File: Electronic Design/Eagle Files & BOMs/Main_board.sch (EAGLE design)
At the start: 49 parts, among them IC2 ATMEGA328-PU, IC3 LM2576S, Q1 BSS192P, Q2 FQD7P20, X1 16MHz

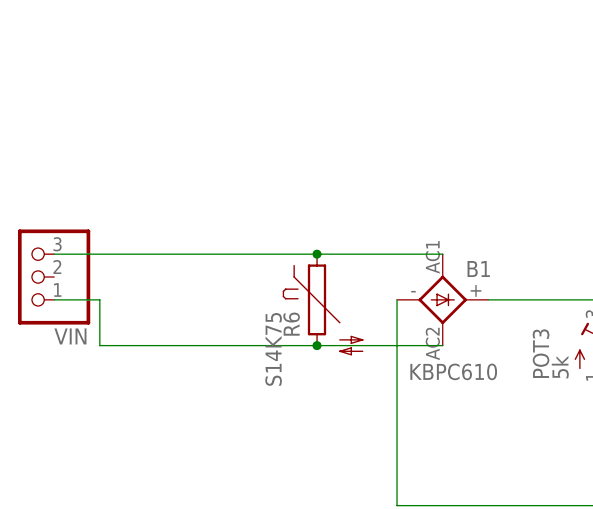
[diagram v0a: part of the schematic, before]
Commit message: Moving everything into postion and adding fuse to start of circuit
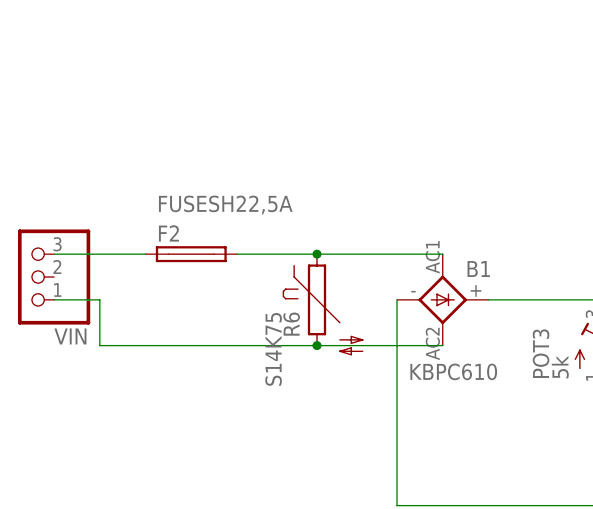
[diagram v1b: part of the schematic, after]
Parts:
- added F2: FUSESH22,5A, fuse:FUSESH22,5A
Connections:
- new net N$1: F2.1, VIN.3
- net VIN_AC1: now also F2.2; no longer VIN.3
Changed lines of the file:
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@@
 <part name="Q1" library="Samson" deviceset="BSS192P" device=""/>
 <part name="Q2" library="Samson" deviceset="FQD7P20" device=""/>
+<part name="F2" library="fuse" deviceset="FUSE" device="SH22,5A" value="FUSESH22,5A"/>
 </parts>
 <sheets>
@@
 <instance part="Q1" gate="G$1" x="-52.07" y="81.28" rot="MR180"/>
 <instance part="Q2" gate="G$1" x="-41.91" y="86.36" rot="R90"/>
+<instance part="F2" gate="G$1" x="-111.76" y="93.98" smashed="yes">
+<attribute name="NAME" x="-115.57" y="95.377" size="1.778" layer="95"/>
+<attribute name="VALUE" x="-115.57" y="98.679" size="1.778" layer="96"/>
+</instance>
 </instances>
 <busses>
@@
 <net name="VIN_AC1" class="0">
 <segment>
-<pinref part="VIN" gate="A" pin="3"/>
-<wire x1="-127" y1="93.98" x2="-97.79" y2="93.98" width="0.1524" layer="91"/>
 <pinref part="R6" gate="G$1" pin="1"/>
 <pinref part="B1" gate="1" pin="AC1"/>
 <wire x1="-83.82" y1="93.98" x2="-97.79" y2="93.98" width="0.1524" layer="91"/>
+<pinref part="F2" gate="G$1" pin="2"/>
+<wire x1="-106.68" y1="93.98" x2="-97.79" y2="93.98" width="0.1524" layer="91"/>
 <junction x="-97.79" y="93.98"/>
 </segment>
@@
 </segment>
 </net>
+<net name="N$1" class="0">
+<segment>
+<pinref part="VIN" gate="A" pin="3"/>
+<pinref part="F2" gate="G$1" pin="1"/>
+<wire x1="-127" y1="93.98" x2="-116.84" y2="93.98" width="0.1524" layer="91"/>
+</segment>
+</net>

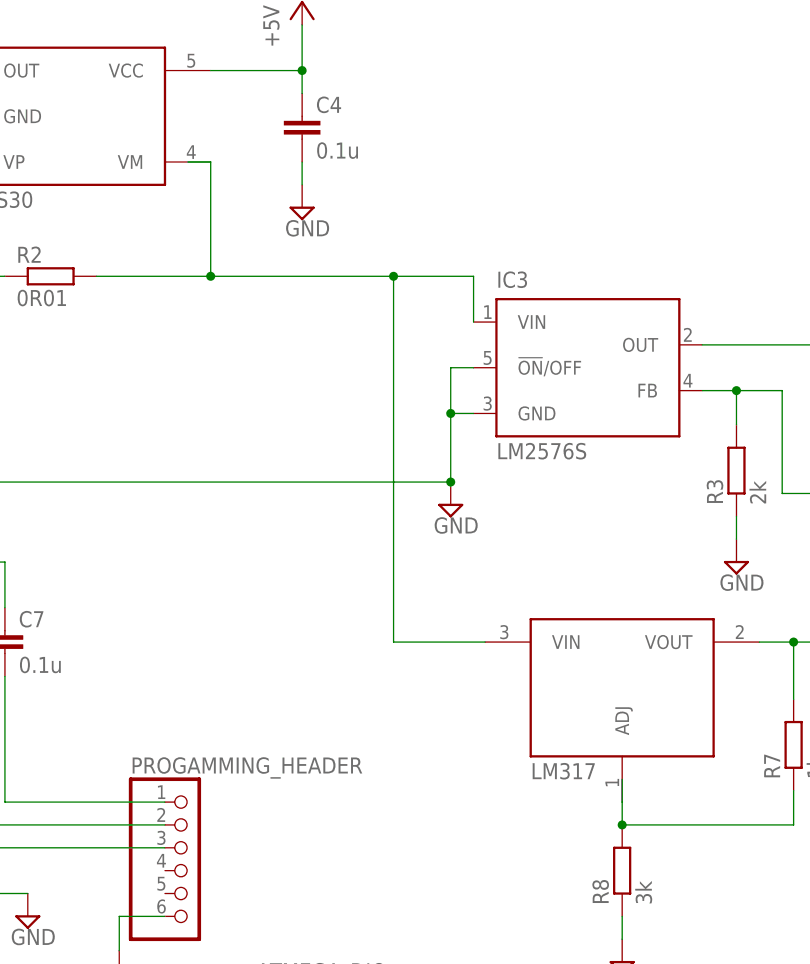
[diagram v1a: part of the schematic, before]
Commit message: moving everything into place and DRC check complete
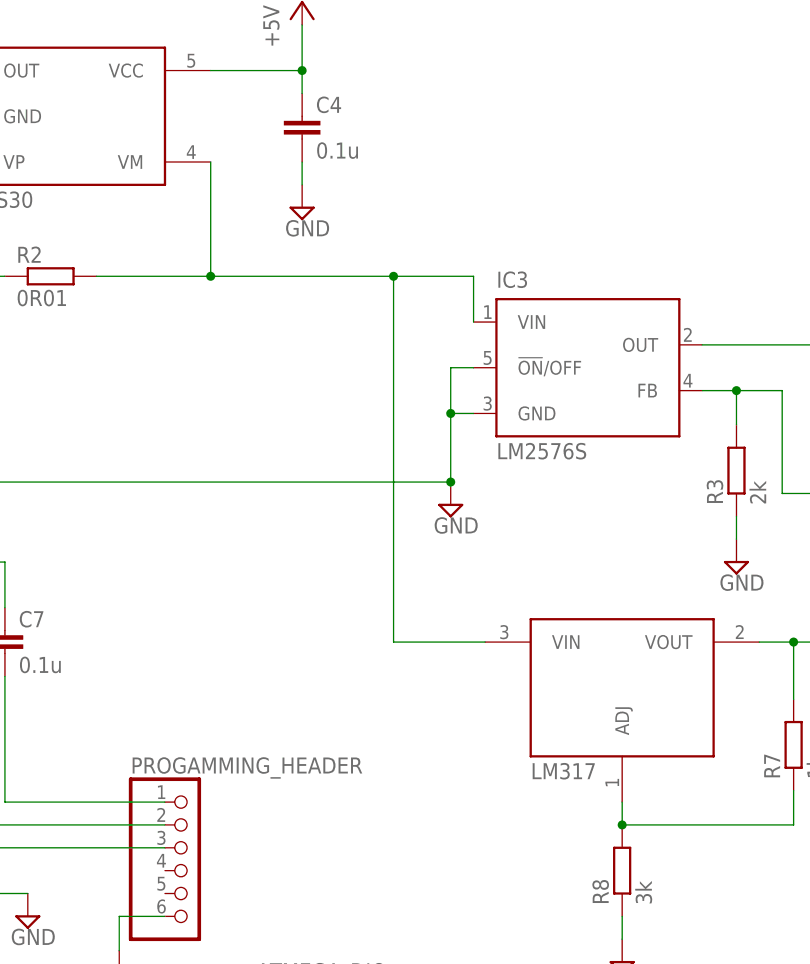
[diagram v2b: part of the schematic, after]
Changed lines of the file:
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@@
 <pinref part="U$1" gate="G$1" pin="VIN"/>
 <pinref part="U$2" gate="G$1" pin="VM"/>
-<wire x1="38.1" y1="101.6" x2="40.64" y2="101.6" width="0.1524" layer="91"/>
 <wire x1="40.64" y1="101.6" x2="40.64" y2="88.9" width="0.1524" layer="91"/>
 <junction x="40.64" y="88.9"/>
@@
 <net name="N$23" class="0">
 <segment>
-<wire x1="86.36" y1="33.02" x2="86.36" y2="30.48" width="0.1524" layer="91"/>
 <pinref part="R7" gate="G$1" pin="1"/>
 <wire x1="86.36" y1="30.48" x2="86.36" y2="27.94" width="0.1524" layer="91"/>

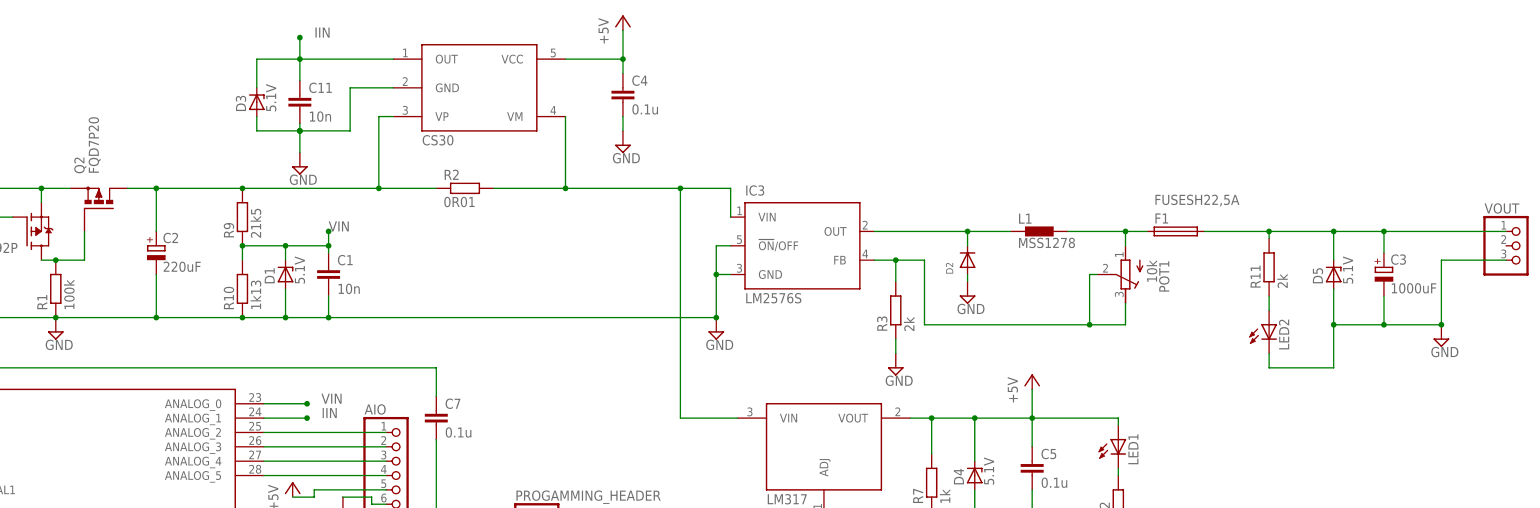
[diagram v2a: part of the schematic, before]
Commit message: Moving buck converter and re-arranging other components as needed
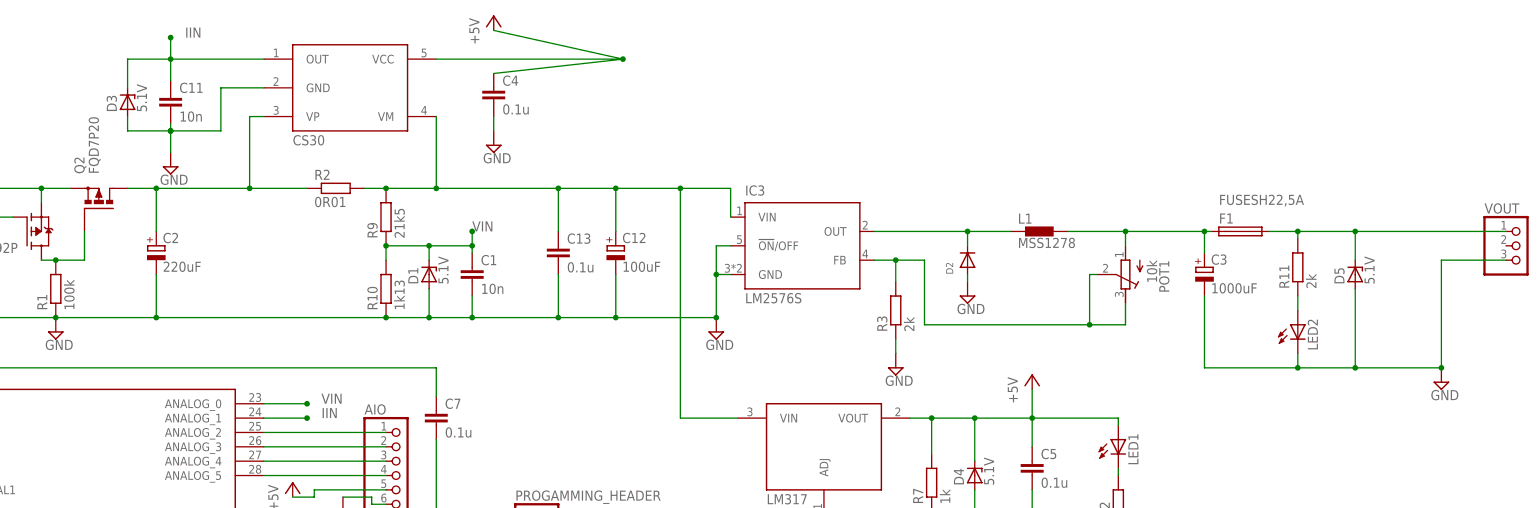
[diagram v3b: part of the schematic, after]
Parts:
- added C12: 100uF, resistor:CPOL-EUE3.5-8
- added C13: 0.1u, resistor:C-EUC1206K
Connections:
- net GND: now also C12.-, C13.2
- net VIN_CURRENT_MEASURED: now also C12.+, C13.1, R9.2
- net VIN_PROTECTED: no longer R9.2
- net VOUT_FINAL: no longer C3.+
- net VOUT_PREFUSE: now also C3.+
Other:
- moved on the sheet: C1, C11, C3, C4, D1, D3, D5, F1, IC3, LED2, R10, R11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

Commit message: Tidying up ground planes and traces. Adding ground stitching vias
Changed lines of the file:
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@@
 <setting verticaltext="up"/>
 </settings>
-<grid distance="0.05" unitdist="inch" unit="inch" style="lines" multiple="1" display="no" altdistance="0.01" altunitdist="inch" altunit="inch"/>
+<grid distance="0.1" unitdist="inch" unit="inch" style="lines" multiple="1" display="no" altdistance="0.01" altunitdist="inch" altunit="inch"/>
 <layers>
-<layer number="1" name="Top" color="4" fill="1" visible="yes" active="no"/>
-<layer number="16" name="Bottom" color="1" fill="1" visible="yes" active="no"/>
-<layer number="17" name="Pads" color="2" fill="1" visible="yes" active="no"/>
-<layer number="18" name="Vias" color="2" fill="1" visible="yes" active="no"/>
-<layer number="19" name="Unrouted" color="6" fill="1" visible="yes" active="no"/>
-<layer number="20" name="Dimension" color="15" fill="1" visible="yes" active="no"/>
-<layer number="21" name="tPlace" color="7" fill="1" visible="yes" active="no"/>
-<layer number="22" name="bPlace" color="7" fill="1" visible="yes" active="no"/>
-<layer number="23" name="tOrigins" color="15" fill="1" visible="yes" active="no"/>
-<layer number="24" name="bOrigins" color="15" fill="1" visible="yes" active="no"/>
-<layer number="25" name="tNames" color="7" fill="1" visible="yes" active="no"/>
-<layer number="26" name="bNames" color="7" fill="1" visible="yes" active="no"/>
-<layer number="27" name="tValues" color="7" fill="1" visible="yes" active="no"/>
-<layer number="28" name="bValues" color="7" fill="1" visible="yes" active="no"/>
+<layer number="1" name="Top" color="4" fill="1" visible="no" active="no"/>
+<layer number="16" name="Bottom" color="1" fill="1" visible="no" active="no"/>
+<layer number="17" name="Pads" color="2" fill="1" visible="no" active="no"/>
+<layer number="18" name="Vias" color="2" fill="1" visible="no" active="no"/>
+<layer number="19" name="Unrouted" color="6" fill="1" visible="no" active="no"/>
+<layer number="20" name="Dimension" color="15" fill="1" visible="no" active="no"/>
+<layer number="21" name="tPlace" color="7" fill="1" visible="no" active="no"/>
+<layer number="22" name="bPlace" color="7" fill="1" visible="no" active="no"/>
+<layer number="23" name="tOrigins" color="15" fill="1" visible="no" active="no"/>
+<layer number="24" name="bOrigins" color="15" fill="1" visible="no" active="no"/>
+<layer number="25" name="tNames" color="7" fill="1" visible="no" active="no"/>
+<layer number="26" name="bNames" color="7" fill="1" visible="no" active="no"/>
+<layer number="27" name="tValues" color="7" fill="1" visible="no" active="no"/>
+<layer number="28" name="bValues" color="7" fill="1" visible="no" active="no"/>
 <layer number="29" name="tStop" color="7" fill="3" visible="no" active="no"/>
 <layer number="30" name="bStop" color="7" fill="6" visible="no" active="no"/>
@@
 <layer number="35" name="tGlue" color="7" fill="4" visible="no" active="no"/>
 <layer number="36" name="bGlue" color="7" fill="5" visible="no" active="no"/>
-<layer number="37" name="tTest" color="7" fill="1" visible="yes" active="no"/>
-<layer number="38" name="bTest" color="7" fill="1" visible="yes" active="no"/>
+<layer number="37" name="tTest" color="7" fill="1" visible="no" active="no"/>
+<layer number="38" name="bTest" color="7" fill="1" visible="no" active="no"/>
 <layer number="39" name="tKeepout" color="4" fill="11" visible="no" active="no"/>
 <layer number="40" name="bKeepout" color="1" fill="11" visible="no" active="no"/>
@@
 <layer number="44" name="Drills" color="7" fill="1" visible="no" active="no"/>
 <layer number="45" name="Holes" color="7" fill="1" visible="no" active="no"/>
-<layer number="46" name="Milling" color="3" fill="1" visible="yes" active="no"/>
-<layer number="47" name="Measures" color="7" fill="1" visible="yes" active="no"/>
-<layer number="48" name="Document" color="7" fill="1" visible="yes" active="no"/>
-<layer number="49" name="Reference" color="7" fill="1" visible="yes" active="no"/>
-<layer number="50" name="dxf" color="7" fill="1" visible="yes" active="no"/>
-<layer number="51" name="tDocu" color="7" fill="1" visible="yes" active="no"/>
-<layer number="52" name="bDocu" color="7" fill="1" visible="yes" active="no"/>
-<layer number="53" name="tGND_GNDA" color="7" fill="9" visible="yes" active="no"/>
-<layer number="54" name="bGND_GNDA" color="1" fill="9" visible="yes" active="no"/>
-<layer number="56" name="wert" color="7" fill="1" visible="yes" active="no"/>
-<layer number="57" name="tCAD" color="7" fill="1" visible="yes" active="no"/>
-<layer number="59" name="tCarbon" color="7" fill="1" visible="yes" active="no"/>
-<layer number="60" name="bCarbon" color="7" fill="1" visible="yes" active="no"/>
+<layer number="46" name="Milling" color="3" fill="1" visible="no" active="no"/>
+<layer number="47" name="Measures" color="7" fill="1" visible="no" active="no"/>
+<layer number="48" name="Document" color="7" fill="1" visible="no" active="no"/>
+<layer number="49" name="Reference" color="7" fill="1" visible="no" active="no"/>
+<layer number="50" name="dxf" color="7" fill="1" visible="no" active="no"/>
+<layer number="51" name="tDocu" color="7" fill="1" visible="no" active="no"/>
+<layer number="52" name="bDocu" color="7" fill="1" visible="no" active="no"/>
+<layer number="53" name="tGND_GNDA" color="7" fill="9" visible="no" active="no"/>
+<layer number="54" name="bGND_GNDA" color="1" fill="9" visible="no" active="no"/>
+<layer number="56" name="wert" color="7" fill="1" visible="no" active="no"/>
+<layer number="57" name="tCAD" color="7" fill="1" visible="no" active="no"/>
+<layer number="59" name="tCarbon" color="7" fill="1" visible="no" active="no"/>
+<layer number="60" name="bCarbon" color="7" fill="1" visible="no" active="no"/>
 <layer number="90" name="Modules" color="5" fill="1" visible="yes" active="yes"/>
 <layer number="91" name="Nets" color="2" fill="1" visible="yes" active="yes"/>
@@
 </segment>
 <segment>
-<wire x1="50.8" y1="111.76" x2="27.94" y2="116.84" width="0.1524" layer="91"/>
+<wire x1="27.94" y1="111.76" x2="27.94" y2="116.84" width="0.1524" layer="91"/>
 <pinref part="+3V2" gate="1" pin="+5V"/>
 <pinref part="U$2" gate="G$1" pin="VCC"/>
-<wire x1="50.8" y1="111.76" x2="17.78" y2="111.76" width="0.1524" layer="91"/>
+<wire x1="27.94" y1="111.76" x2="17.78" y2="111.76" width="0.1524" layer="91"/>
 <pinref part="C4" gate="G$1" pin="1"/>
-<wire x1="50.8" y1="111.76" x2="27.94" y2="109.22" width="0.1524" layer="91"/>
-<junction x="50.8" y="111.76"/>
+<wire x1="27.94" y1="111.76" x2="27.94" y2="109.22" width="0.1524" layer="91"/>
+<junction x="27.94" y="111.76"/>
 </segment>
 </net>

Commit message: tidying up component names on silkscreen
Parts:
- renumbered LED1 to UC_PWR, LED2 to PWR
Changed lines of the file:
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@@
 <part name="SUPPLY13" library="supply2" deviceset="GND" device=""/>
 <part name="D5" library="diode" deviceset="ZPD" device="" value="5.1V"/>
-<part name="LED1" library="adafruit" deviceset="LED" device="SMT1206"/>
-<part name="LED2" library="adafruit" deviceset="LED" device="SMT1206"/>
+<part name="UC_PWR" library="adafruit" deviceset="LED" device="SMT1206"/>
+<part name="PWR" library="adafruit" deviceset="LED" device="SMT1206"/>
 <part name="R11" library="resistor" deviceset="R-EU_" device="R1206" value="2k"/>
 <part name="R12" library="resistor" deviceset="R-EU_" device="R1206" value="2k"/>
@@
 <instance part="SUPPLY13" gate="GND" x="113.03" y="24.13"/>
 <instance part="D5" gate="G$1" x="180.34" y="73.66" rot="R90"/>
-<instance part="LED1" gate="G$1" x="138.43" y="44.45"/>
-<instance part="LED2" gate="G$1" x="170.18" y="64.77"/>
+<instance part="UC_PWR" gate="G$1" x="138.43" y="44.45"/>
+<instance part="PWR" gate="G$1" x="170.18" y="64.77"/>
 <instance part="R11" gate="G$1" x="170.18" y="74.93" rot="R90"/>
 <instance part="R12" gate="G$1" x="138.43" y="33.02" rot="R90"/>
@@
 <pinref part="D5" gate="G$1" pin="A"/>
 <wire x1="180.34" y1="71.12" x2="180.34" y2="57.15" width="0.1524" layer="91"/>
-<pinref part="LED2" gate="G$1" pin="C"/>
+<pinref part="PWR" gate="G$1" pin="C"/>
 <wire x1="170.18" y1="59.69" x2="170.18" y2="57.15" width="0.1524" layer="91"/>
 <wire x1="170.18" y1="57.15" x2="180.34" y2="57.15" width="0.1524" layer="91"/>
@@
 <pinref part="D4" gate="G$1" pin="C"/>
 <wire x1="113.03" y1="40.64" x2="113.03" y2="48.26" width="0.1524" layer="91"/>
-<pinref part="LED1" gate="G$1" pin="A"/>
+<pinref part="UC_PWR" gate="G$1" pin="A"/>
 <wire x1="123.19" y1="48.26" x2="138.43" y2="48.26" width="0.1524" layer="91"/>
 <wire x1="138.43" y1="48.26" x2="138.43" y2="46.99" width="0.1524" layer="91"/>
@@
 <segment>
 <pinref part="R11" gate="G$1" pin="1"/>
-<pinref part="LED2" gate="G$1" pin="A"/>
+<pinref part="PWR" gate="G$1" pin="A"/>
 <wire x1="170.18" y1="69.85" x2="170.18" y2="67.31" width="0.1524" layer="91"/>
 </segment>
@@
 <net name="N$28" class="0">
 <segment>
-<pinref part="LED1" gate="G$1" pin="C"/>
+<pinref part="UC_PWR" gate="G$1" pin="C"/>
 <pinref part="R12" gate="G$1" pin="2"/>
 <wire x1="138.43" y1="39.37" x2="138.43" y2="38.1" width="0.1524" layer="91"/>

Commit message: Don't know
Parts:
- POT3: value 5k -> 100k
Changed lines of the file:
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@@
 <part name="C1" library="resistor" deviceset="C-EU" device="C1206K" value="10n"/>
 <part name="C2" library="resistor" deviceset="CPOL-EU" device="E3.5-10" value="220uF"/>
-<part name="POT3" library="resistor" deviceset="R-TRIMM" device="3296W" value="5k"/>
+<part name="POT3" library="resistor" deviceset="R-TRIMM" device="3296W" value="100k"/>
 <part name="R1" library="resistor" deviceset="R-EU_" device="0207/10" value="100k"/>
 <part name="SUPPLY22" library="supply2" deviceset="GND" device=""/>
